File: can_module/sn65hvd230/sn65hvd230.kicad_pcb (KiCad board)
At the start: 2 copper layers, 41 x 14 mm, 5 parts, among them J1 Conn_01x04, J2 Conn_01x02, U1 SN65HVD230

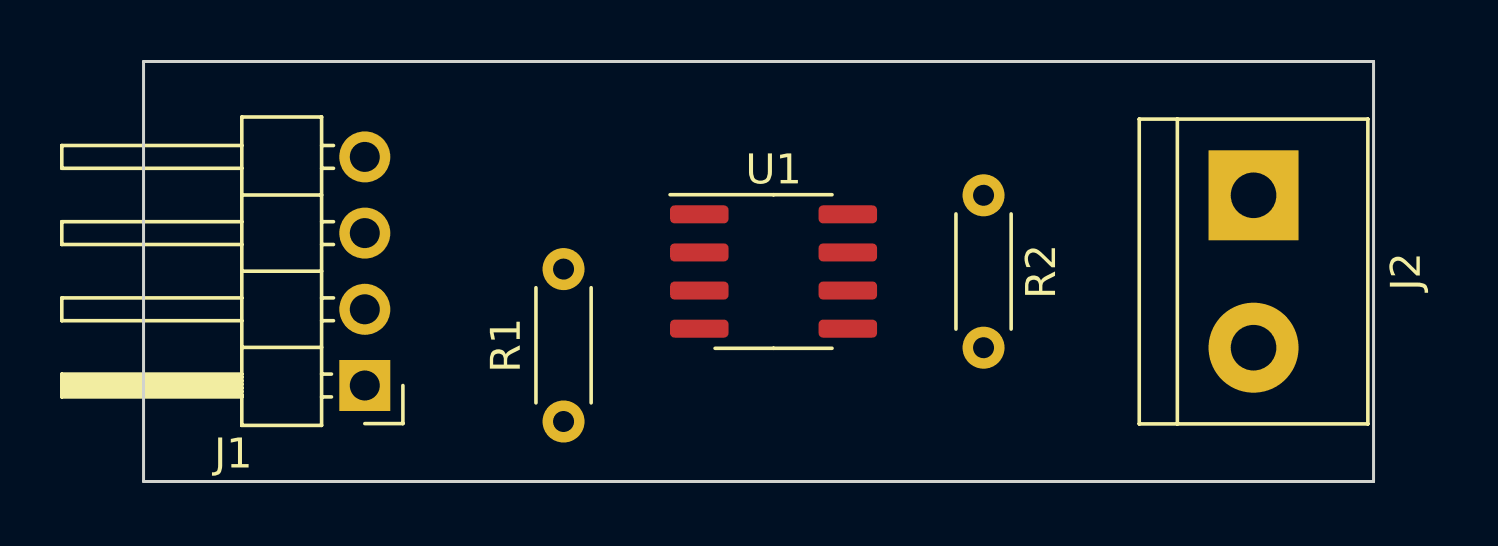
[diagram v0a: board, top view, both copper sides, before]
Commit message: update to can module
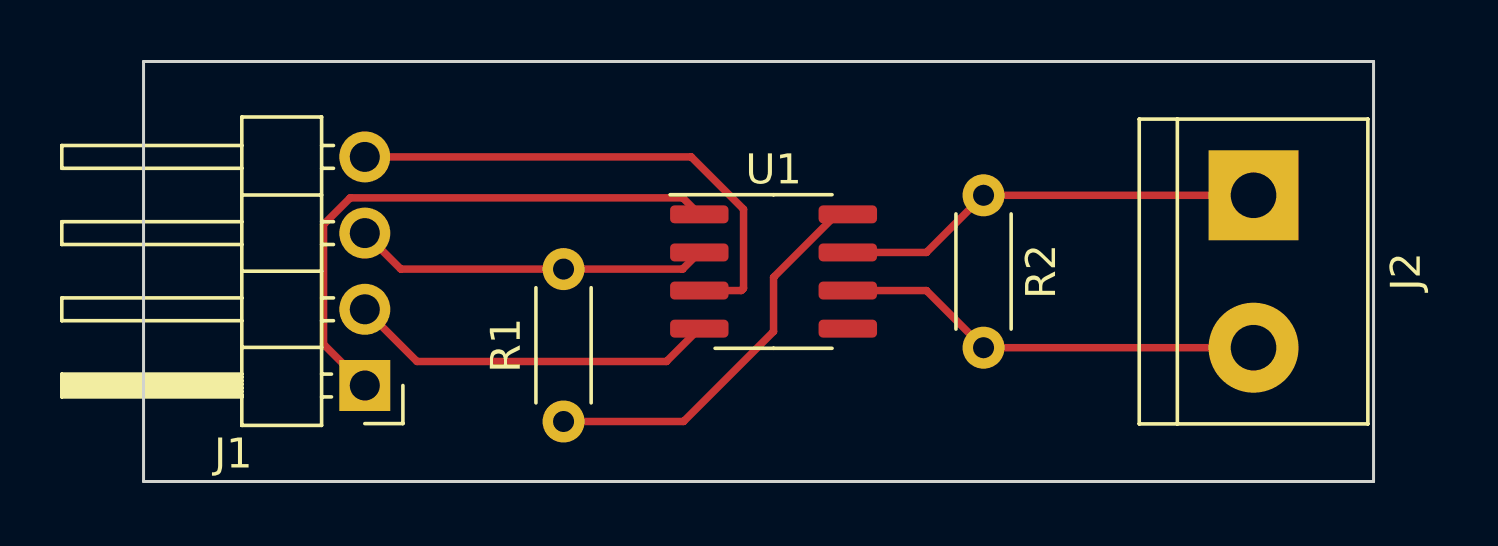
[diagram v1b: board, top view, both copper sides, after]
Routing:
- net /D: track 0.00 -> 19.1 mm
- net Net-(J1-Pad4): track 0.00 -> 17.5 mm
- net /CANL: track 0.00 -> 14.3 mm
- net /CANH: track 0.00 -> 14.3 mm
- net Net-(R1-Pad1): track 0.00 -> 13.4 mm
- net /R: track 0.00 -> 12.3 mm
- net GND: track 0.00 -> 11.9 mm
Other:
- board text added: "CANH"
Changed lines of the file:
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@@
   (gr_rect (start 180 107) (end 139 93) (layer "Edge.Cuts") (width 0.1) (fill none))
   (gr_rect (start 180 107) (end 139 93) (layer "User.1") (width 0.15) (fill none))
+  (gr_text "CANH" (at 172 97) (layer "B.SilkS")
+    (effects (font (size 1 1) (thickness 0.15)) (justify mirror))
+  )
+  (segment (start 145.888501 97.545489) (end 145 98.43399) (width 0.25) (layer "F.Cu") (net 1))
+  (segment (start 156.975489 97.545489) (end 145.888501 97.545489) (width 0.25) (layer "F.Cu") (net 1))
+  (segment (start 145 98.43399) (end 145 102.425) (width 0.25) (layer "F.Cu") (net 1))
+  (segment (start 145 102.425) (end 146.375 103.8) (width 0.25) (layer "F.Cu") (net 1))
+  (segment (start 157.525 98.095) (end 156.975489 97.545489) (width 0.25) (layer "F.Cu") (net 1))
+  (segment (start 146.375 101.26) (end 148.115 103) (width 0.25) (layer "F.Cu") (net 2))
+  (segment (start 148.115 103) (end 156.43 103) (width 0.25) (layer "F.Cu") (net 2))
+  (segment (start 156.43 103) (end 157.525 101.905) (width 0.25) (layer "F.Cu") (net 2))
+  (segment (start 153 99.92) (end 147.575 99.92) (width 0.25) (layer "F.Cu") (net 3))
+  (segment (start 156.97 99.92) (end 153 99.92) (width 0.25) (layer "F.Cu") (net 3))
+  (segment (start 157.525 99.365) (end 156.97 99.92) (width 0.25) (layer "F.Cu") (net 3))
+  (segment (start 147.575 99.92) (end 146.375 98.72) (width 0.25) (layer "F.Cu") (net 3))
+  (segment (start 146.375 96.18) (end 157.256072 96.18) (width 0.25) (layer "F.Cu") (net 4))
+  (segment (start 159 100.55821) (end 158.92321 100.635) (width 0.25) (layer "F.Cu") (net 4))
+  (segment (start 157.256072 96.18) (end 159 97.923928) (width 0.25) (layer "F.Cu") (net 4))
+  (segment (start 159 97.923928) (end 159 100.55821) (width 0.25) (layer "F.Cu") (net 4))
+  (segment (start 158.92321 100.635) (end 157.525 100.635) (width 0.25) (layer "F.Cu") (net 4))
+  (segment (start 167 97.46) (end 176 97.46) (width 0.25) (layer "F.Cu") (net 5))
+  (segment (start 165.095 99.365) (end 167 97.46) (width 0.25) (layer "F.Cu") (net 5))
+  (segment (start 162.475 99.365) (end 165.095 99.365) (width 0.25) (layer "F.Cu") (net 5))
+  (segment (start 167 102.54) (end 165.095 100.635) (width 0.25) (layer "F.Cu") (net 6))
+  (segment (start 176 102.54) (end 167 102.54) (width 0.25) (layer "F.Cu") (net 6))
+  (segment (start 165.095 100.635) (end 162.475 100.635) (width 0.25) (layer "F.Cu") (net 6))
+  (segment (start 157 105) (end 153 105) (width 0.25) (layer "F.Cu") (net 7))
+  (segment (start 162.098928 98.095) (end 160 100.193928) (width 0.25) (layer "F.Cu") (net 7))
+  (segment (start 162.475 98.095) (end 162.098928 98.095) (width 0.25) (layer "F.Cu") (net 7))
+  (segment (start 160 102) (end 157 105) (width 0.25) (layer "F.Cu") (net 7))
+  (segment (start 160 100.193928) (end 160 102) (width 0.25) (layer "F.Cu") (net 7))
 )
